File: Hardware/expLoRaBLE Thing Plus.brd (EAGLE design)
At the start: 22.9 x 58.4 mm, 144 parts, among them J2 CORTEX_DEBUG, J5 USB Female Type C Connector, J6 QWIIC_RIGHT_ANGLE, J8 U.FL, U1 MCP73831, U2 3.3V, U3 NM180100, U4 CH340E_MSOP10, U6 DPX202700DT-4162A1, Y1 32.768kHz

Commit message: v10 production gerbers
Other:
- board text added: "v10"
- board text removed: "v02"
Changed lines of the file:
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@@
 <dimension x1="0" y1="2.54" x2="22.86" y2="2.54" x3="11.43" y3="-8.89" textsize="1.27" layer="47" unit="inch" visible="yes"/>
 <dimension x1="2.54" y1="0" x2="2.54" y2="58.42" x3="-8.89" y3="29.21" textsize="1.27" layer="47" unit="inch"/>
-<text x="11.43" y="0.3175" size="1.27" layer="16" font="vector" ratio="15" rot="MR0" align="bottom-center">v02</text>
+<text x="11.43" y="0.3175" size="1.27" layer="16" font="vector" ratio="15" rot="MR0" align="bottom-center">v10</text>
 <text x="-30.48" y="-39.37" size="5.08" layer="51" font="vector">4-LAYER BOARD</text>
 <text x="0.635" y="17.78" size="0.8128" layer="1" font="vector" ratio="25">1</text>

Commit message: changed RTS jumper to normally closed trace
-bumped version to v11 in brd and sch
-adjusted RTS jumper paragraph in sch
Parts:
- RTS: value JUMPER-SMT_2_NO_SILK -> JUMPER-SMT_2_NC_TRACE_SILK; device SparkFun-Jumpers:SMT-JUMPER_2_NO_SILK -> SparkFun-Jumpers:SMT-JUMPER_2_NC_TRACE_SILK
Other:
- board text added: "v11"
- board text removed: "v10"
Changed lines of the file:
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@@
 <layers>
 <layer number="1" name="Top" color="4" fill="1" visible="yes" active="yes"/>
-<layer number="2" name="Route2" color="11" fill="3" visible="yes" active="yes"/>
+<layer number="2" name="Route2" color="11" fill="3" visible="no" active="yes"/>
 <layer number="3" name="Route3" color="17" fill="1" visible="no" active="no"/>
 <layer number="4" name="Route4" color="18" fill="1" visible="no" active="no"/>
@@
 <layer number="13" name="Route13" color="21" fill="1" visible="no" active="no"/>
 <layer number="14" name="Route14" color="22" fill="1" visible="no" active="no"/>
-<layer number="15" name="Route15" color="13" fill="6" visible="yes" active="yes"/>
+<layer number="15" name="Route15" color="13" fill="6" visible="no" active="yes"/>
 <layer number="16" name="Bottom" color="1" fill="1" visible="yes" active="yes"/>
 <layer number="17" name="Pads" color="2" fill="1" visible="yes" active="yes"/>
@@
 <layer number="47" name="Measures" color="7" fill="1" visible="no" active="yes"/>
 <layer number="48" name="Document" color="7" fill="1" visible="no" active="yes"/>
-<layer number="49" name="Reference" color="7" fill="1" visible="yes" active="yes"/>
+<layer number="49" name="Reference" color="7" fill="1" visible="no" active="yes"/>
 <layer number="50" name="dxf" color="7" fill="1" visible="no" active="no"/>
 <layer number="51" name="tDocu" color="6" fill="1" visible="yes" active="yes"/>
@@
 <dimension x1="0" y1="2.54" x2="22.86" y2="2.54" x3="11.43" y3="-8.89" textsize="1.27" layer="47" unit="inch" visible="yes"/>
 <dimension x1="2.54" y1="0" x2="2.54" y2="58.42" x3="-8.89" y3="29.21" textsize="1.27" layer="47" unit="inch"/>
-<text x="11.43" y="0.3175" size="1.27" layer="16" font="vector" ratio="15" rot="MR0" align="bottom-center">v10</text>
+<text x="11.43" y="0.3175" size="1.27" layer="16" font="vector" ratio="15" rot="MR0" align="bottom-center">v11</text>
 <text x="-30.48" y="-39.37" size="5.08" layer="51" font="vector">4-LAYER BOARD</text>
 <text x="0.635" y="17.78" size="0.8128" layer="1" font="vector" ratio="25">1</text>
@@
 <attribute name="VALUE" x="17.3228" y="25.4762" size="0.6096" layer="27" font="vector" ratio="20" rot="R270" align="top-center"/>
 </element>
-<element name="RTS" library="SparkFun-Jumpers" library_urn="urn:adsk.eagle:library:528" package="SMT-JUMPER_2_NO_SILK" package3d_urn="urn:adsk.eagle:package:39279/1" value="JUMPER-SMT_2_NO_SILK" x="15.24" y="21.59" smashed="yes" rot="MR270">
+<element name="RTS" library="SparkFun-Jumpers" package="SMT-JUMPER_2_NC_TRACE_SILK" package3d_urn="urn:adsk.eagle:package:39281/1" value="JUMPER-SMT_2_NC_TRACE_SILK" x="15.24" y="21.59" smashed="yes" rot="MR270">
 <attribute name="NAME" x="14.097" y="21.59" size="0.6096" layer="26" font="vector" ratio="20" rot="MR270" align="bottom-center"/>
 <attribute name="VALUE" x="16.383" y="21.59" size="0.6096" layer="28" font="vector" ratio="20" rot="MR270" align="top-center"/>
@@
 <contactref element="RTS" pad="2"/>
 <wire x1="16.8402" y1="19.0246" x2="15.24" y2="20.6248" width="0.2032" layer="16"/>
-<wire x1="15.24" y1="21.1836" x2="15.24" y2="20.6248" width="0.2032" layer="16"/>
+<wire x1="15.24" y1="21.0693" x2="15.24" y2="20.6248" width="0.2032" layer="16"/>
 <wire x1="16.8402" y1="19.0246" x2="16.8402" y2="18.2118" width="0.2032" layer="16"/>
 <wire x1="16.8402" y1="13.9954" x2="16.8402" y2="15.5457" width="0.2032" layer="1"/>
@@
 <contactref element="C1" pad="2"/>
 <contactref element="RTS" pad="1"/>
-<wire x1="15.24" y1="21.9964" x2="15.24" y2="23.6474" width="0.2032" layer="16"/>
+<wire x1="15.24" y1="22.1107" x2="15.24" y2="23.6474" width="0.2032" layer="16"/>
 <via x="16.2052" y="24.6126" extent="1-16" drill="0.3048"/>
 <wire x1="16.2052" y1="24.6126" x2="18.0712" y2="24.6126" width="0.2032" layer="1"/>

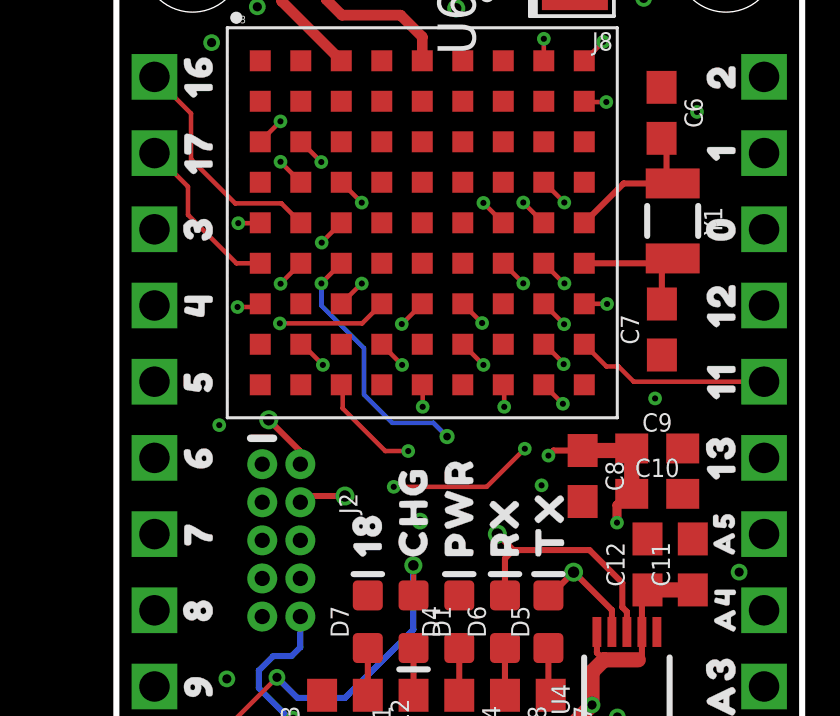
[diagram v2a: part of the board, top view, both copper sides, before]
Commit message: UART pin change
-changed UART pin selection to match "standard" sparkfun SVL bootloader
-TXO:GPIO48, RXI:GPIO49
-Note, also moved "D10" net/button to GPIO4. This will also need to be configured with a custom "info zero" file to configure ASB to work.
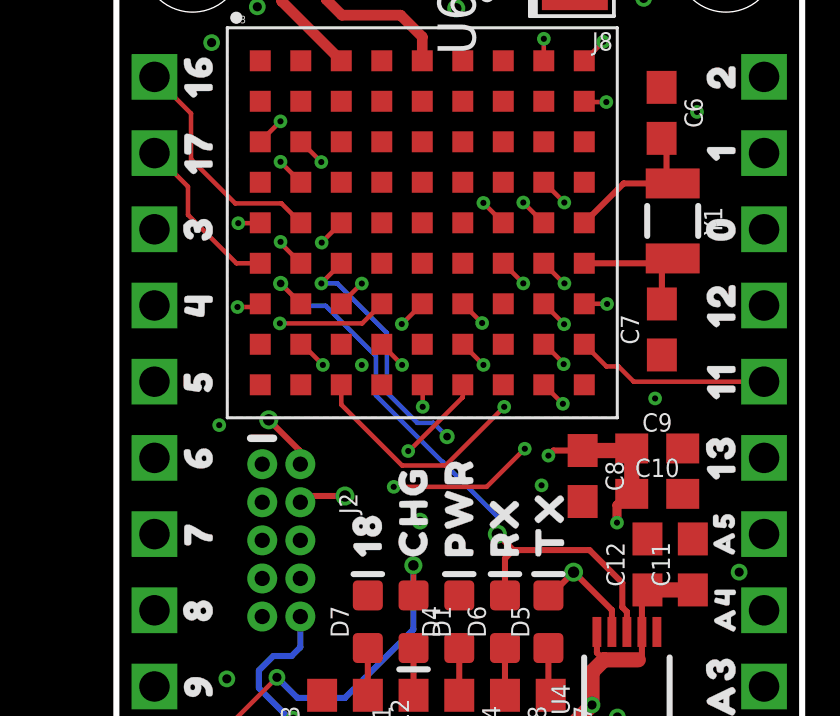
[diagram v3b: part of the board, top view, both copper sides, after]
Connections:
- net D10/SWCH: now also U3.J6; no longer U3.J3
- net RXI-0: now also U3.G2; no longer U3.D3
- net TXO-0: now also U3.J3; no longer U3.J7
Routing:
- net TXO-0: track 11.0 -> 18.0 mm
- net RXI-0: track 23.9 -> 20.9 mm
- net ~D7: track 14.8 -> 17.3 mm
- net D10/SWCH: track 40.2 -> 39.6 mm
- net ~D6: track 9.61 -> 10.1 mm
- net GND: vias 27 -> 28

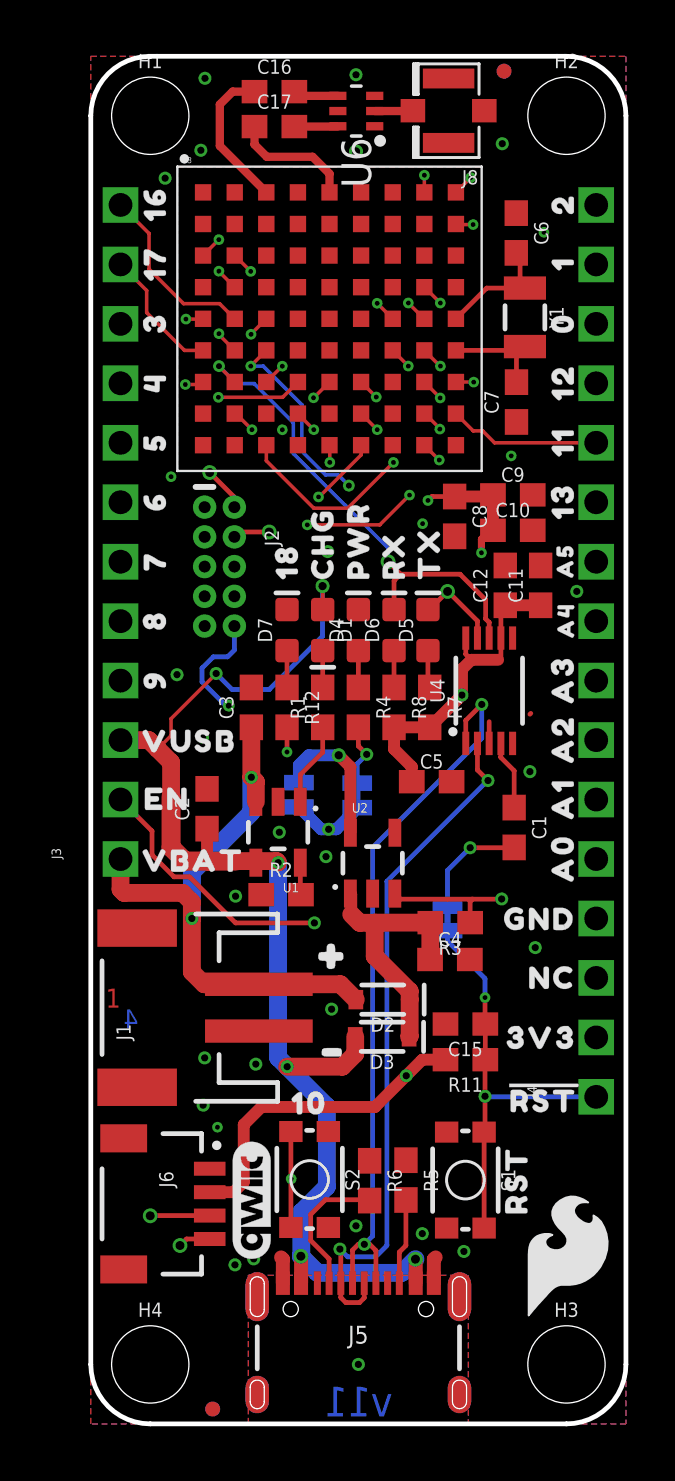
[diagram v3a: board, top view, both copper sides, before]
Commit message: Added Boot net/pin (for ASB)
-chose a boot pin (GPIO22). Note, we could not use the standard SFE pin of GPIO47, but this can be set during production programming of custom "info.0" binary.
-connected RTS (post closed jumper) to boot net, including C13 and pull down R10.
-left D10 on GPIO4 and is separate from boot circuit. It is soley a user button, similar to the Artemis Thing Plus design (although on a different GPIO#).
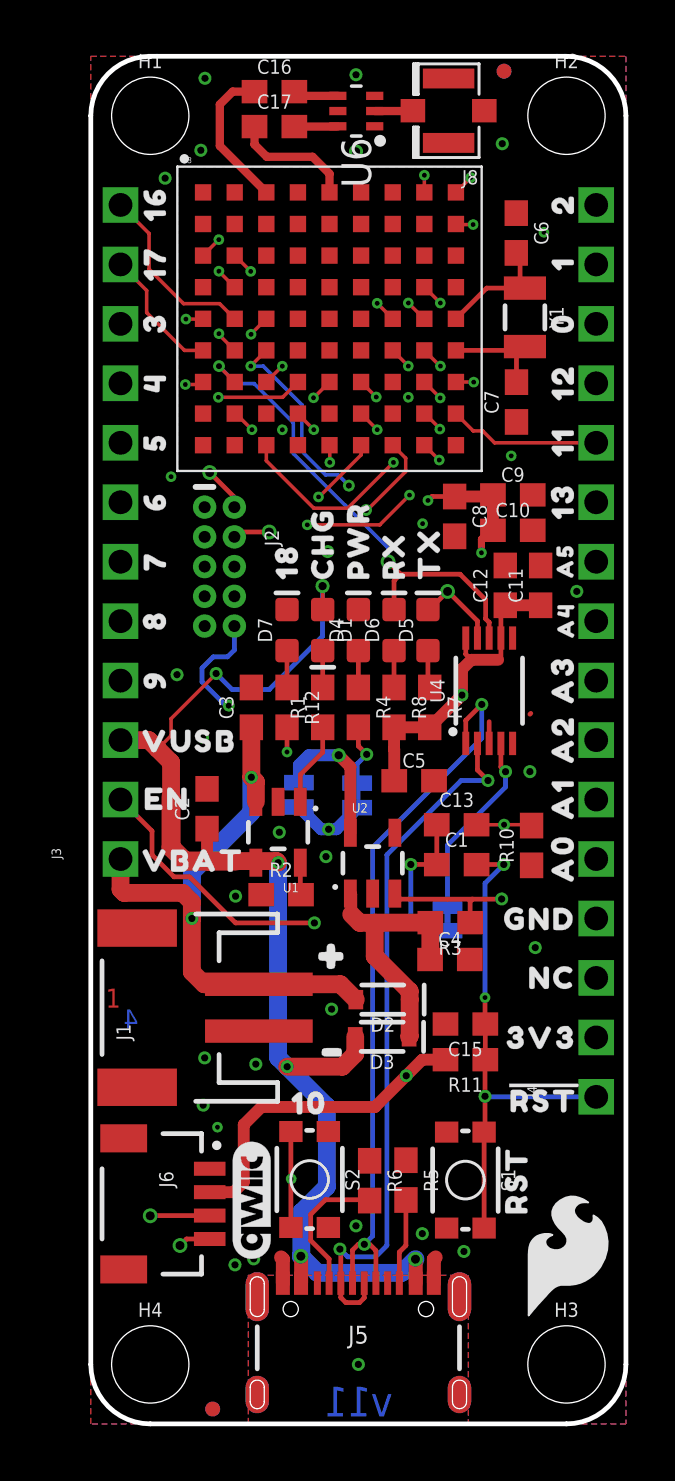
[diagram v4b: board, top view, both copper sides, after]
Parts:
- added C13: 0.1uF, SparkFun-Capacitors:0603
- added R10: 220k, SparkFun-Resistors:0603
- moved C1 2.92 mm to (15.6, 23.9), turned to 0 degrees
- moved C5 0.75 mm to (13.8, 27.5)
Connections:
- new net BOOT: C13.2, R10.2, U3.J7
- net !RESET: now also C1.2; no longer RTS.2
- net !RTS: now also RTS.1; no longer C1.1
- net GND: now also R10.1
- net N$15: now also C1.1, C13.1, RTS.2; no longer C1.2, RTS.1
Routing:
- net BOOT: track 0.00 -> 22.5 mm, vias 0 -> 2
- net !RTS: track 2.98 -> 8.07 mm, vias 0 -> 1
- net !RESET: track 65.5 -> 69.1 mm, vias 4 -> 5
- net N$15: track 4.79 -> 6.93 mm
- net D-1: track 29.7 -> 30.3 mm
- net GND: vias 28 -> 29
